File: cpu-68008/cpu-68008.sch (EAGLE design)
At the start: 65 parts, among them IC1 68008, IC11 NE555, IC2 AS6C4008, IC3 39SF010, IC4 DS1244Y, IC5 XR68C681, Q1 8MHz, Q3 3.6864 MHz

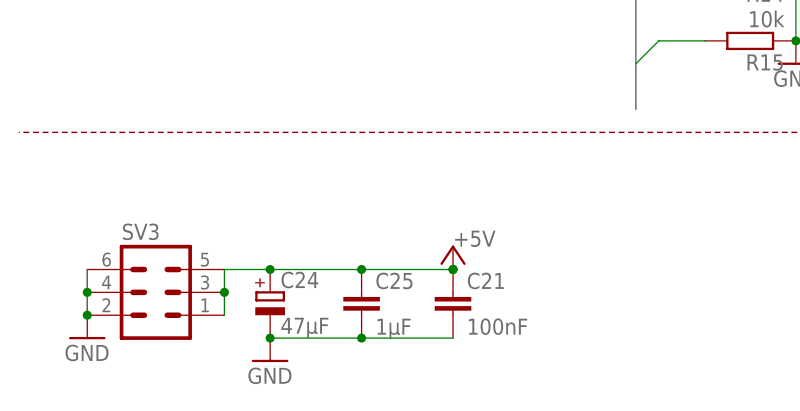
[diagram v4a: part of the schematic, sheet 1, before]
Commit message: finish routng
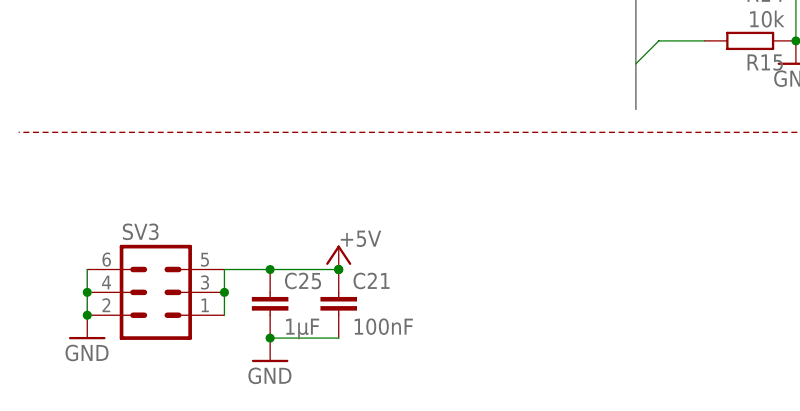
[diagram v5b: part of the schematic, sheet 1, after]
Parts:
- removed C24: 47µF, rcl:CPOL-EUCT6032
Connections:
- net +5V: no longer C24.+
- net GND: no longer C24.-
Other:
- moved on the sheet: C21, C25
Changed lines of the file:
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@@
 </part>
 <part name="GND26" library="supply1" library_urn="urn:adsk.eagle:library:371" deviceset="GND" device=""/>
-<part name="C24" library="rcl" library_urn="urn:adsk.eagle:library:334" deviceset="CPOL-EU" device="CT6032" package3d_urn="urn:adsk.eagle:package:23305/2" value="47µF">
-<spice>
-<pinmapping spiceprefix="C">
-<pinmap gate="G$1" pin="+" pinorder="1"/>
-<pinmap gate="G$1" pin="-" pinorder="2"/>
-</pinmapping>
-</spice>
-<attribute name="MOUSER" value="581-TAJD476M016RNJV"/>
-</part>
 <part name="C25" library="rcl" library_urn="urn:adsk.eagle:library:334" deviceset="C-EU" device="C0805" package3d_urn="urn:adsk.eagle:package:23617/2" value="1µF">
 <attribute name="MOUSER" value="710-885012107015"/>
@@
 <attribute name="VALUE" x="234.823" y="173.2026" size="1.778" layer="96"/>
 </instance>
-<instance part="C24" gate="G$1" x="27.94" y="17.78" smashed="yes">
-<attribute name="MOUSER" x="27.94" y="17.78" size="1.27" layer="96" display="off"/>
-<attribute name="NAME" x="29.083" y="18.2626" size="1.778" layer="95"/>
-<attribute name="VALUE" x="29.083" y="13.1826" size="1.778" layer="96"/>
-</instance>
-<instance part="C25" gate="G$1" x="38.1" y="17.78" smashed="yes">
-<attribute name="MOUSER" x="38.1" y="17.78" size="1.27" layer="96" align="top-center" display="off"/>
-<attribute name="NAME" x="39.624" y="18.161" size="1.778" layer="95"/>
-<attribute name="VALUE" x="39.624" y="13.081" size="1.778" layer="96"/>
-</instance>
-<instance part="P+24" gate="1" x="48.26" y="22.86" smashed="yes">
-<attribute name="VALUE" x="48.26" y="22.86" size="1.778" layer="96"/>
+<instance part="C25" gate="G$1" x="27.94" y="17.78" smashed="yes">
+<attribute name="MOUSER" x="27.94" y="17.78" size="1.27" layer="96" align="top-center" display="off"/>
+<attribute name="NAME" x="29.464" y="18.161" size="1.778" layer="95"/>
+<attribute name="VALUE" x="29.464" y="13.081" size="1.778" layer="96"/>
+</instance>
+<instance part="P+24" gate="1" x="35.56" y="22.86" smashed="yes">
+<attribute name="VALUE" x="35.56" y="22.86" size="1.778" layer="96"/>
 </instance>
 <instance part="R13" gate="G$1" x="124.46" y="17.78" smashed="yes">
@@
 <attribute name="VALUE" x="5.08" y="10.16" size="1.778" layer="96"/>
 </instance>
-<instance part="C21" gate="G$1" x="48.26" y="17.78" smashed="yes">
-<attribute name="MOUSER" x="48.26" y="17.78" size="1.27" layer="96" align="top-center" display="off"/>
-<attribute name="NAME" x="49.784" y="18.161" size="1.778" layer="95"/>
-<attribute name="VALUE" x="49.784" y="13.081" size="1.778" layer="96"/>
+<instance part="C21" gate="G$1" x="35.56" y="17.78" smashed="yes">
+<attribute name="MOUSER" x="35.56" y="17.78" size="1.27" layer="96" align="top-center" display="off"/>
+<attribute name="NAME" x="37.084" y="18.161" size="1.778" layer="95"/>
+<attribute name="VALUE" x="37.084" y="13.081" size="1.778" layer="96"/>
 </instance>
 <instance part="GND29" gate="1" x="27.94" y="10.16" smashed="yes">
@@
 <junction x="22.86" y="17.78"/>
 <wire x1="22.86" y1="20.32" x2="27.94" y2="20.32" width="0.1524" layer="91"/>
-<pinref part="C24" gate="G$1" pin="+"/>
-<wire x1="27.94" y1="20.32" x2="38.1" y2="20.32" width="0.1524" layer="91"/>
+<pinref part="C25" gate="G$1" pin="1"/>
+<wire x1="27.94" y1="20.32" x2="35.56" y2="20.32" width="0.1524" layer="91"/>
 <junction x="27.94" y="20.32"/>
-<pinref part="C25" gate="G$1" pin="1"/>
-<wire x1="38.1" y1="20.32" x2="48.26" y2="20.32" width="0.1524" layer="91"/>
-<junction x="38.1" y="20.32"/>
 <pinref part="P+24" gate="1" pin="+5V"/>
-<junction x="48.26" y="20.32"/>
+<junction x="35.56" y="20.32"/>
 <pinref part="C21" gate="G$1" pin="1"/>
-<junction x="48.26" y="20.32"/>
+<junction x="35.56" y="20.32"/>
 </segment>
 <segment>
@@
 <segment>
 <pinref part="C25" gate="G$1" pin="2"/>
-<wire x1="38.1" y1="12.7" x2="27.94" y2="12.7" width="0.1524" layer="91"/>
-<pinref part="C24" gate="G$1" pin="-"/>
-<junction x="38.1" y="12.7"/>
+<junction x="27.94" y="12.7"/>
 <pinref part="C21" gate="G$1" pin="2"/>
-<wire x1="48.26" y1="12.7" x2="38.1" y2="12.7" width="0.1524" layer="91"/>
+<wire x1="35.56" y1="12.7" x2="27.94" y2="12.7" width="0.1524" layer="91"/>
 <pinref part="GND29" gate="1" pin="GND"/>
-<junction x="27.94" y="12.7"/>
-</segment>
-<segment>
+</segment>
+<segment>

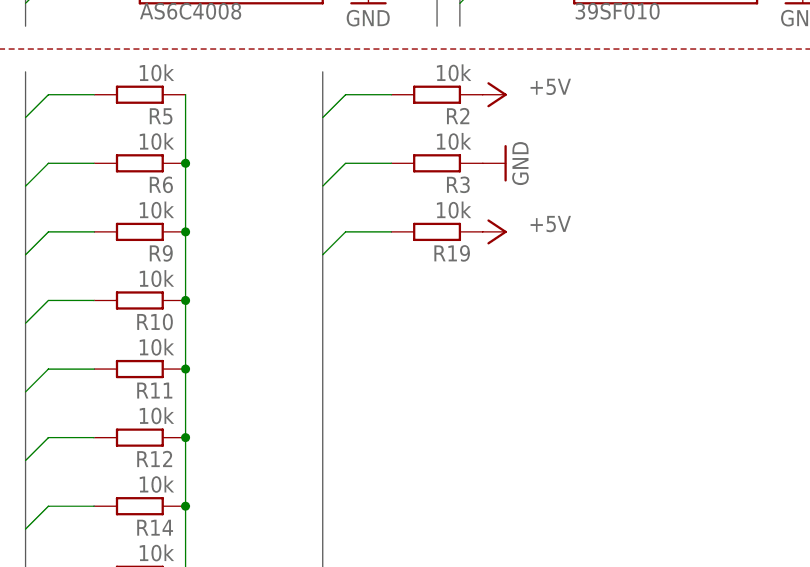
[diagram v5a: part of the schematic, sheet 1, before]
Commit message: a few routing improvements
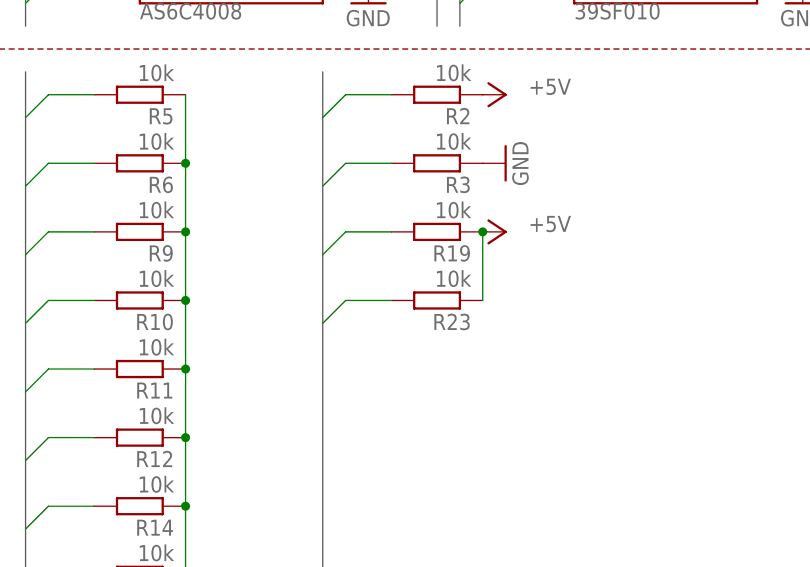
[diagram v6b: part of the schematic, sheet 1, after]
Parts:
- added R23: 10k, rcl:R-EU_R2012
- IC6: value (none) -> ATF1504AS
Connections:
- net !BERR: now also R23.2
- net +5V: now also R23.1
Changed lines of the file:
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@@
 </part>
 <part name="IC2" library="68komputer" deviceset="AS6C4008" device="" package3d_urn="urn:adsk.eagle:package:18076/2" value="AS6C4008"/>
-<part name="IC6" library="68komputer" deviceset="ATF1504AS" device="PLCC44-SOCKET"/>
+<part name="IC6" library="68komputer" deviceset="ATF1504AS" device="PLCC44-SOCKET" value="ATF1504AS"/>
 <part name="P+3" library="supply1" library_urn="urn:adsk.eagle:library:371" deviceset="+5V" device=""/>
 <part name="GND9" library="supply1" library_urn="urn:adsk.eagle:library:371" deviceset="GND" device=""/>
@@
 <part name="C22" library="rcl" library_urn="urn:adsk.eagle:library:334" deviceset="C-EU" device="C0805" package3d_urn="urn:adsk.eagle:package:23617/2" value="100nF">
 <attribute name="MOUSER" value="710-885012207072"/>
+</part>
+<part name="R23" library="rcl" library_urn="urn:adsk.eagle:library:334" deviceset="R-EU_" device="R2012" package3d_urn="urn:adsk.eagle:package:23543/2" value="10k">
+<spice>
+<pinmapping spiceprefix="R">
+<pinmap gate="G$1" pin="1" pinorder="1"/>
+<pinmap gate="G$1" pin="2" pinorder="2"/>
+</pinmapping>
+</spice>
+<attribute name="MOUSER" value="652-CR0805FX-1002ELF"/>
 </part>
 </parts>
@@
 <attribute name="VALUE" x="124.46" y="83.82" size="1.778" layer="96"/>
 </instance>
+<instance part="R23" gate="G$1" x="114.3" y="76.2" smashed="yes" rot="R180">
+<attribute name="NAME" x="118.11" y="74.7014" size="1.778" layer="95" rot="R180"/>
+<attribute name="VALUE" x="118.11" y="79.502" size="1.778" layer="96" rot="R180"/>
+<attribute name="MOUSER" x="114.3" y="76.2" size="1.778" layer="96" rot="R180" align="top-left" display="off"/>
+</instance>
 </instances>
 <busses>
@@
 </segment>
 </bus>
-<bus name="!BG,!BR,!VPA">
+<bus name="!BERR,!BG,!BR,!VPA">
 <segment>
 <wire x1="101.6" y1="101.6" x2="101.6" y2="38.1" width="0.762" layer="92"/>
@@
 <pinref part="R19" gate="G$1" pin="1"/>
 <pinref part="P+19" gate="1" pin="+5V"/>
+<pinref part="R23" gate="G$1" pin="1"/>
+<wire x1="119.38" y1="83.82" x2="119.38" y2="76.2" width="0.1524" layer="91"/>
+<junction x="119.38" y="83.82"/>
 </segment>
 </net>
@@
 <wire x1="12.7" y1="147.32" x2="10.16" y2="144.78" width="0.1524" layer="91"/>
 </segment>
-</net>
+<segment>
+<pinref part="R23" gate="G$1" pin="2"/>
+<wire x1="109.22" y1="76.2" x2="104.14" y2="76.2" width="0.1524" layer="91"/>
+<wire x1="104.14" y1="76.2" x2="101.6" y2="73.66" width="0.1524" layer="91"/>
+</segment>
+</net>

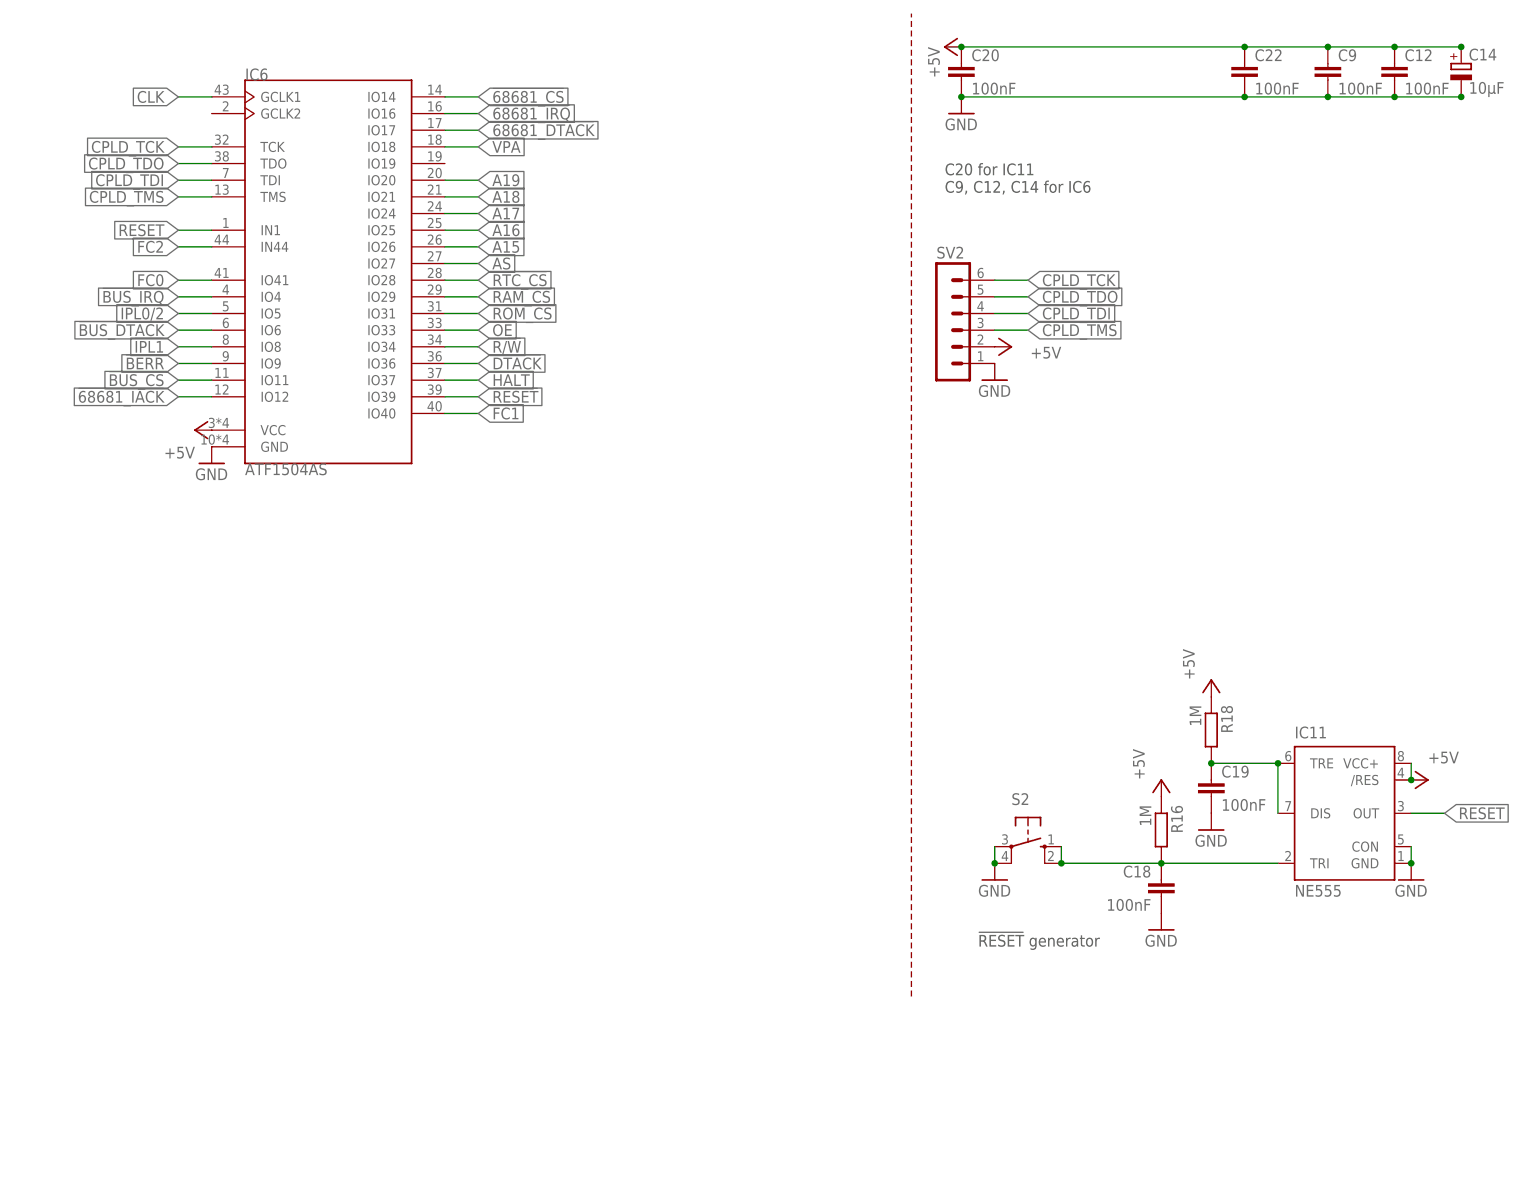
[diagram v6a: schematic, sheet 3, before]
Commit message: replaced CPLD with PLDs
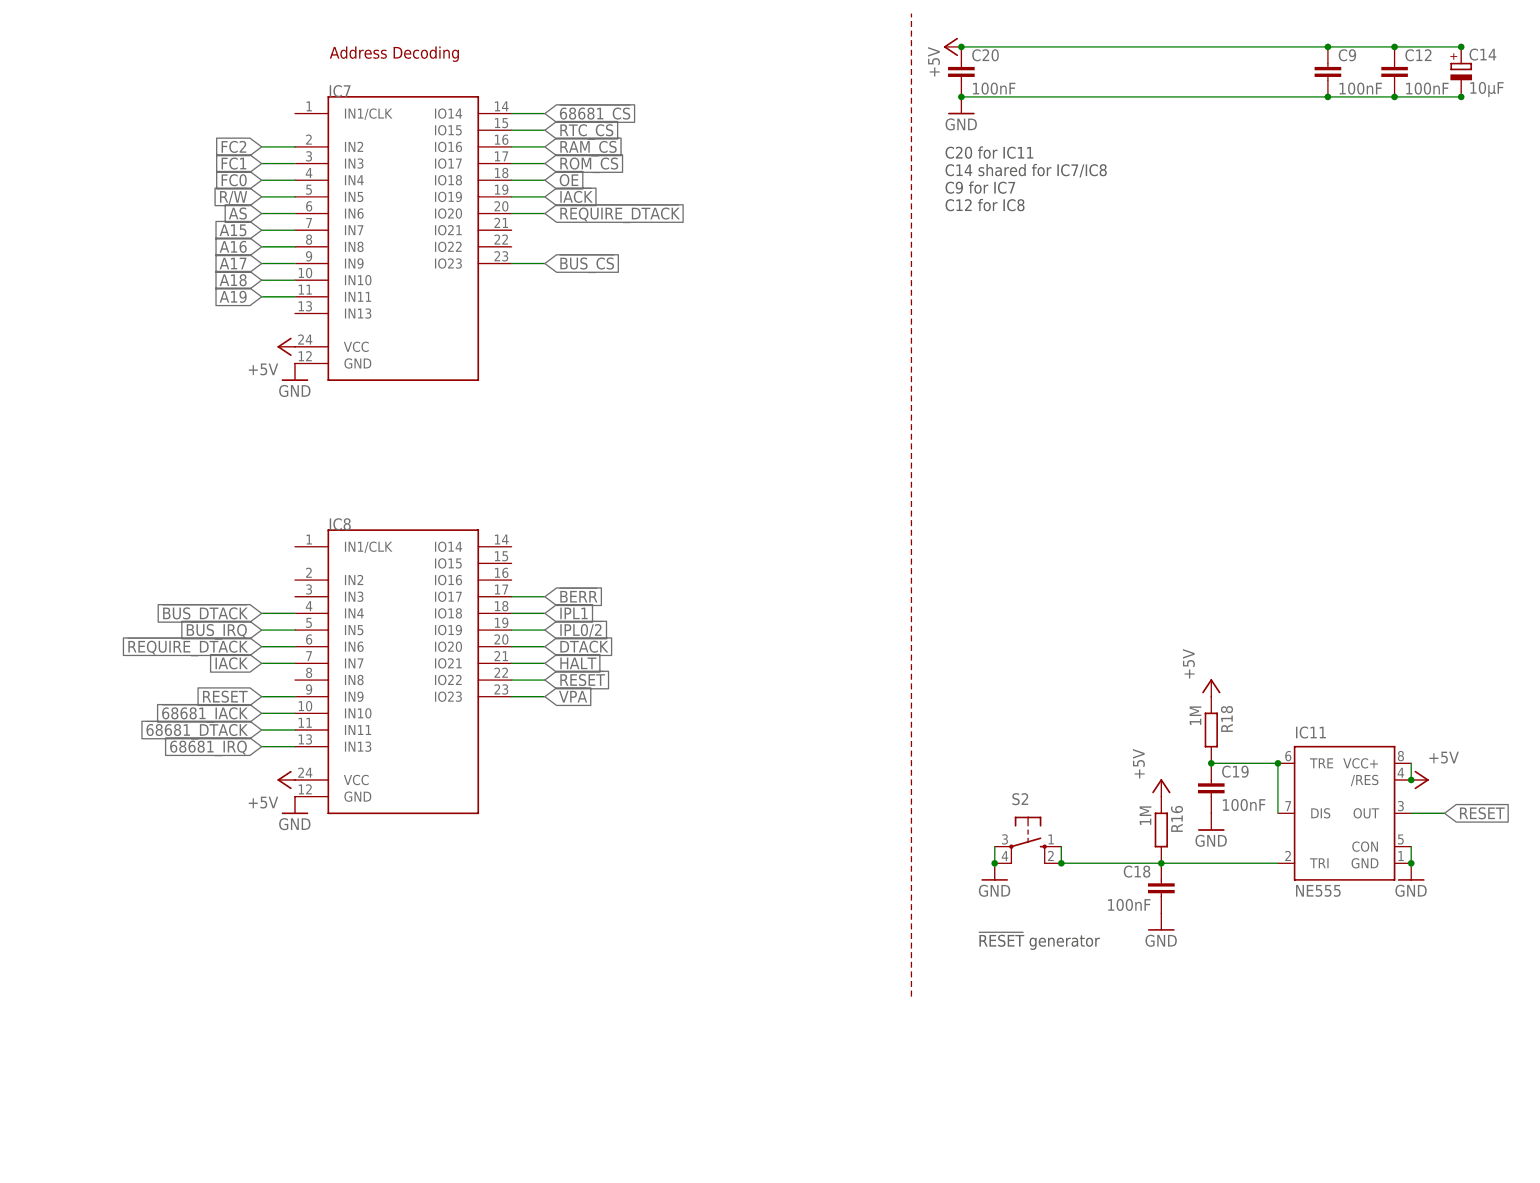
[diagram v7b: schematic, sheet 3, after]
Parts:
- removed C22: 100nF, rcl:C-EUC0805
- removed IC6: ATF1504AS, 68komputer:ATF1504ASPLCC44-SOCKET
- removed SV2: (no value), con-lstb:MA06-1
- added IC7, IC8: (no value), 68komputer:GAL22V10DIP24
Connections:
- removed net CPLD_TCK: IC6.TCK, SV2.6
- removed net CPLD_TDI: IC6.TDI, SV2.4
- removed net CPLD_TDO: IC6.TDO, SV2.5
- removed net CPLD_TMS: IC6.TMS, SV2.3
- new net !IACK: IC7.IO19, IC8.IN7
- new net !REQUIRE_DTACK: IC7.IO20, IC8.IN6
- net !68681_CS: now also IC7.IO14; no longer IC6.IO14
- net !68681_DTACK: now also IC8.IN11; no longer IC6.IO17
- net !68681_IACK: now also IC8.IN10; no longer IC6.IO12
- net !68681_IRQ: now also IC8.IN13; no longer IC6.IO16
- net !AS: now also IC7.IN6; no longer IC6.IO27
- net !BERR: now also IC8.IO17; no longer IC6.IO9
- net !BUS_CS: now also IC7.IO23; no longer IC6.IO11
- net !BUS_DTACK: now also IC8.IN4; no longer IC6.IO6
- net !BUS_IRQ: now also IC8.IN5; no longer IC6.IO4
- net !DTACK: now also IC8.IO20; no longer IC6.IO36
- net !HALT: now also IC8.IO21; no longer IC6.IO37
- net !IPL0/2: now also IC8.IO19; no longer IC6.IO5
- net !IPL1: now also IC8.IO18; no longer IC6.IO8
- net !OE: now also IC7.IO18; no longer IC6.IO33
- net !RAM_CS: now also IC7.IO16; no longer IC6.IO29
- net !RESET: now also IC8.IO22; no longer IC6.IO39
- net !ROM_CS: now also IC7.IO17; no longer IC6.IO31
- net !RTC_CS: now also IC7.IO15; no longer IC6.IO28
- net !VPA: now also IC8.IO23; no longer IC6.IO18
- net +5V: now also IC7.VCC, IC8.VCC; no longer C22.1, IC6.VCC, SV2.2
- net A15: now also IC7.IN7; no longer IC6.IO26
- net A16: now also IC7.IN8; no longer IC6.IO25
- net A17: now also IC7.IN9; no longer IC6.IO24
- net A18: now also IC7.IN10; no longer IC6.IO21
- net A19: now also IC7.IN11; no longer IC6.IO20
- net CLK: no longer IC6.GCLK1
- net FC0: now also IC7.IN4; no longer IC6.IO41
- net FC1: now also IC7.IN3; no longer IC6.IO40
- net FC2: now also IC7.IN2; no longer IC6.IN44
- net GND: now also IC7.GND, IC8.GND; no longer C22.2, IC6.GND, SV2.1
- net R/!W!: now also IC7.IN5; no longer IC6.IO34
- net RESET: now also IC8.IN9; no longer IC6.IN1
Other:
- note added: "Address Decoding"
- note added: "C20 for IC11 C14 shared for IC7/IC8 C9 for IC7 C12 for IC8"
- note removed: "C20 for IC11 C9, C12, C14 for IC6"
